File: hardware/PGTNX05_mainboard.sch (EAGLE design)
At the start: 174 parts, among them IC1 H11L1, IC2 LM2574N-5.0, IC3 40106N, IC4 H11L1

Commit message: Added correct diode type BZX55C12
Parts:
- D2, D3: value (none) -> BZX55C12

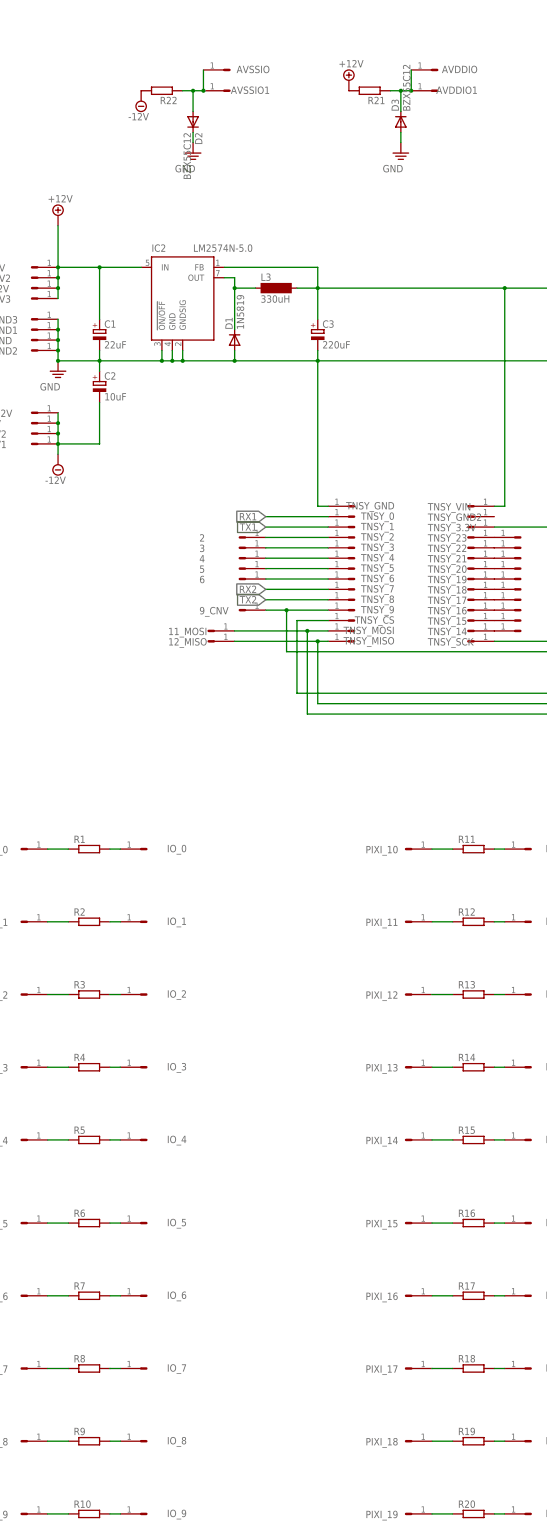
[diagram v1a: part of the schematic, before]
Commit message: Add resistor values
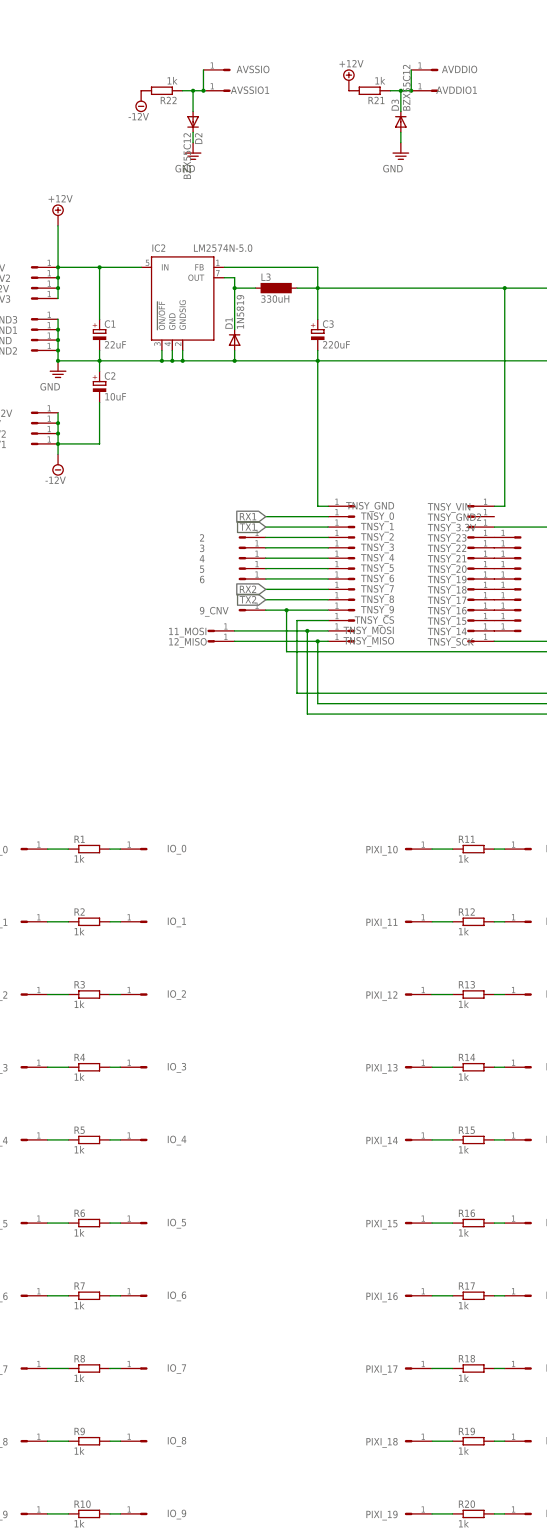
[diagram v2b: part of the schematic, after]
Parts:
- R1, R10, R11, R12, R13, R14, R15, R16, R17, R18, R19, R2, R20, R21, R22, R3, R4, R5, R6, R7, R8, R9: value (none) -> 1k
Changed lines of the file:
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@@
 <attribute name="SPICEPREFIX" value="X"/>
 </part>
-<part name="R21" library="resistors" deviceset="RESISTOR" device="RESISTOR/UPRIGHT/7.5"/>
-<part name="R22" library="resistors" deviceset="RESISTOR" device="RESISTOR/UPRIGHT/7.5"/>
+<part name="R21" library="resistors" deviceset="RESISTOR" device="RESISTOR/UPRIGHT/7.5" value="1k"/>
+<part name="R22" library="resistors" deviceset="RESISTOR" device="RESISTOR/UPRIGHT/7.5" value="1k"/>
 <part name="D2" library="transistors" deviceset="1N4148" device="DO35-7" value="BZX55C12"/>
 <part name="SUPPLY10" library="supply" deviceset="+12V" device="">
@@
 <attribute name="SPICEPREFIX" value="X"/>
 </part>
-<part name="R1" library="resistors" deviceset="RESISTOR" device="RESISTOR/UPRIGHT/7.5"/>
+<part name="R1" library="resistors" deviceset="RESISTOR" device="RESISTOR/UPRIGHT/7.5" value="1k"/>
 <part name="IO_0" library="connectors" deviceset="HEADER/MALE/01" device="">
 <attribute name="SPICEPREFIX" value="X"/>
@@
 <attribute name="SPICEPREFIX" value="X"/>
 </part>
-<part name="R2" library="resistors" deviceset="RESISTOR" device="RESISTOR/UPRIGHT/7.5"/>
+<part name="R2" library="resistors" deviceset="RESISTOR" device="RESISTOR/UPRIGHT/7.5" value="1k"/>
 <part name="IO_1" library="connectors" deviceset="HEADER/MALE/01" device="">
 <attribute name="SPICEPREFIX" value="X"/>
@@
 <attribute name="SPICEPREFIX" value="X"/>
 </part>
-<part name="R3" library="resistors" deviceset="RESISTOR" device="RESISTOR/UPRIGHT/7.5"/>
+<part name="R3" library="resistors" deviceset="RESISTOR" device="RESISTOR/UPRIGHT/7.5" value="1k"/>
 <part name="IO_2" library="connectors" deviceset="HEADER/MALE/01" device="">
 <attribute name="SPICEPREFIX" value="X"/>
@@
 <attribute name="SPICEPREFIX" value="X"/>
 </part>
-<part name="R4" library="resistors" deviceset="RESISTOR" device="RESISTOR/UPRIGHT/7.5"/>
+<part name="R4" library="resistors" deviceset="RESISTOR" device="RESISTOR/UPRIGHT/7.5" value="1k"/>
 <part name="IO_3" library="connectors" deviceset="HEADER/MALE/01" device="">
 <attribute name="SPICEPREFIX" value="X"/>
@@
 <attribute name="SPICEPREFIX" value="X"/>
 </part>
-<part name="R5" library="resistors" deviceset="RESISTOR" device="RESISTOR/UPRIGHT/7.5"/>
+<part name="R5" library="resistors" deviceset="RESISTOR" device="RESISTOR/UPRIGHT/7.5" value="1k"/>
 <part name="IO_4" library="connectors" deviceset="HEADER/MALE/01" device="">
 <attribute name="SPICEPREFIX" value="X"/>
@@
 <attribute name="SPICEPREFIX" value="X"/>
 </part>
-<part name="R6" library="resistors" deviceset="RESISTOR" device="RESISTOR/UPRIGHT/7.5"/>
+<part name="R6" library="resistors" deviceset="RESISTOR" device="RESISTOR/UPRIGHT/7.5" value="1k"/>
 <part name="IO_5" library="connectors" deviceset="HEADER/MALE/01" device="">
 <attribute name="SPICEPREFIX" value="X"/>
@@
 <attribute name="SPICEPREFIX" value="X"/>
 </part>
-<part name="R7" library="resistors" deviceset="RESISTOR" device="RESISTOR/UPRIGHT/7.5"/>
+<part name="R7" library="resistors" deviceset="RESISTOR" device="RESISTOR/UPRIGHT/7.5" value="1k"/>
 <part name="IO_6" library="connectors" deviceset="HEADER/MALE/01" device="">
 <attribute name="SPICEPREFIX" value="X"/>
@@
 <attribute name="SPICEPREFIX" value="X"/>
 </part>
-<part name="R8" library="resistors" deviceset="RESISTOR" device="RESISTOR/UPRIGHT/7.5"/>
+<part name="R8" library="resistors" deviceset="RESISTOR" device="RESISTOR/UPRIGHT/7.5" value="1k"/>
 <part name="IO_7" library="connectors" deviceset="HEADER/MALE/01" device="">
 <attribute name="SPICEPREFIX" value="X"/>
@@
 <attribute name="SPICEPREFIX" value="X"/>
 </part>
-<part name="R9" library="resistors" deviceset="RESISTOR" device="RESISTOR/UPRIGHT/7.5"/>
+<part name="R9" library="resistors" deviceset="RESISTOR" device="RESISTOR/UPRIGHT/7.5" value="1k"/>
 <part name="IO_8" library="connectors" deviceset="HEADER/MALE/01" device="">
 <attribute name="SPICEPREFIX" value="X"/>
@@
 <attribute name="SPICEPREFIX" value="X"/>
 </part>
-<part name="R10" library="resistors" deviceset="RESISTOR" device="RESISTOR/UPRIGHT/7.5"/>
+<part name="R10" library="resistors" deviceset="RESISTOR" device="RESISTOR/UPRIGHT/7.5" value="1k"/>
 <part name="IO_9" library="connectors" deviceset="HEADER/MALE/01" device="">
 <attribute name="SPICEPREFIX" value="X"/>
@@
 <attribute name="SPICEPREFIX" value="X"/>
 </part>
-<part name="R11" library="resistors" deviceset="RESISTOR" device="RESISTOR/UPRIGHT/7.5"/>
+<part name="R11" library="resistors" deviceset="RESISTOR" device="RESISTOR/UPRIGHT/7.5" value="1k"/>
 <part name="IO_10" library="connectors" deviceset="HEADER/MALE/01" device="">
 <attribute name="SPICEPREFIX" value="X"/>
@@
 <attribute name="SPICEPREFIX" value="X"/>
 </part>
-<part name="R12" library="resistors" deviceset="RESISTOR" device="RESISTOR/UPRIGHT/7.5"/>
+<part name="R12" library="resistors" deviceset="RESISTOR" device="RESISTOR/UPRIGHT/7.5" value="1k"/>
 <part name="IO_11" library="connectors" deviceset="HEADER/MALE/01" device="">
 <attribute name="SPICEPREFIX" value="X"/>
@@
 <attribute name="SPICEPREFIX" value="X"/>
 </part>
-<part name="R13" library="resistors" deviceset="RESISTOR" device="RESISTOR/UPRIGHT/7.5"/>
+<part name="R13" library="resistors" deviceset="RESISTOR" device="RESISTOR/UPRIGHT/7.5" value="1k"/>
 <part name="IO_12" library="connectors" deviceset="HEADER/MALE/01" device="">
 <attribute name="SPICEPREFIX" value="X"/>
@@
 <attribute name="SPICEPREFIX" value="X"/>
 </part>
-<part name="R14" library="resistors" deviceset="RESISTOR" device="RESISTOR/UPRIGHT/7.5"/>
+<part name="R14" library="resistors" deviceset="RESISTOR" device="RESISTOR/UPRIGHT/7.5" value="1k"/>
 <part name="IO_13" library="connectors" deviceset="HEADER/MALE/01" device="">
 <attribute name="SPICEPREFIX" value="X"/>
@@
 <attribute name="SPICEPREFIX" value="X"/>
 </part>
-<part name="R15" library="resistors" deviceset="RESISTOR" device="RESISTOR/UPRIGHT/7.5"/>
+<part name="R15" library="resistors" deviceset="RESISTOR" device="RESISTOR/UPRIGHT/7.5" value="1k"/>
 <part name="IO_14" library="connectors" deviceset="HEADER/MALE/01" device="">
 <attribute name="SPICEPREFIX" value="X"/>
@@
 <attribute name="SPICEPREFIX" value="X"/>
 </part>
-<part name="R16" library="resistors" deviceset="RESISTOR" device="RESISTOR/UPRIGHT/7.5"/>
+<part name="R16" library="resistors" deviceset="RESISTOR" device="RESISTOR/UPRIGHT/7.5" value="1k"/>
 <part name="IO_15" library="connectors" deviceset="HEADER/MALE/01" device="">
 <attribute name="SPICEPREFIX" value="X"/>
@@
 <attribute name="SPICEPREFIX" value="X"/>
 </part>
-<part name="R17" library="resistors" deviceset="RESISTOR" device="RESISTOR/UPRIGHT/7.5"/>
+<part name="R17" library="resistors" deviceset="RESISTOR" device="RESISTOR/UPRIGHT/7.5" value="1k"/>
 <part name="IO_16" library="connectors" deviceset="HEADER/MALE/01" device="">
 <attribute name="SPICEPREFIX" value="X"/>
@@
 <attribute name="SPICEPREFIX" value="X"/>
 </part>
-<part name="R18" library="resistors" deviceset="RESISTOR" device="RESISTOR/UPRIGHT/7.5"/>
+<part name="R18" library="resistors" deviceset="RESISTOR" device="RESISTOR/UPRIGHT/7.5" value="1k"/>
 <part name="IO_17" library="connectors" deviceset="HEADER/MALE/01" device="">
 <attribute name="SPICEPREFIX" value="X"/>
@@
 <attribute name="SPICEPREFIX" value="X"/>
 </part>
-<part name="R19" library="resistors" deviceset="RESISTOR" device="RESISTOR/UPRIGHT/7.5"/>
+<part name="R19" library="resistors" deviceset="RESISTOR" device="RESISTOR/UPRIGHT/7.5" value="1k"/>
 <part name="IO_18" library="connectors" deviceset="HEADER/MALE/01" device="">
 <attribute name="SPICEPREFIX" value="X"/>
@@
 <attribute name="SPICEPREFIX" value="X"/>
 </part>
-<part name="R20" library="resistors" deviceset="RESISTOR" device="RESISTOR/UPRIGHT/7.5"/>
+<part name="R20" library="resistors" deviceset="RESISTOR" device="RESISTOR/UPRIGHT/7.5" value="1k"/>
 <part name="IO_19" library="connectors" deviceset="HEADER/MALE/01" device="">
 <attribute name="SPICEPREFIX" value="X"/>
